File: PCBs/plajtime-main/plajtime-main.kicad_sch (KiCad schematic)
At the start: 84 parts, among them J1 RP SWD, J2 Internal connector, J3 Display connector, J4 Extention connector, J5 Battery connector, J6 Nordic SWD, U1 W25Q64JWU, U2 MP2664, U3 TPS63031DSK, U4 RP2350A, U5 BMA456, U6 MAX17055, U7 RV-3028-C7, U8 nRF52833_QDxx, U9 W25Q64JWU, Y1 13MHz, Y2 32MHz

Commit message: Some layout is done
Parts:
- removed AE1: Antenna_Chip, RF_Antenna:Johanson_2450AT18x100_2400-2500Mhz, symbol Device:Antenna_Chip
- removed C1, C17, C20: 10uF, Capacitor_SMD:C_0402_1005Metric, symbol Device:C
- removed C5: 0.1uF, Capacitor_SMD:C_0201_0603Metric, symbol Device:C
- removed J4: Extention connector, Library:FPC_7, symbol Connector_Generic_MountingPin:Conn_01x07_MountingPin
- removed J5: Battery connector, Library:CONN8_505004-0812_MOL, symbol Connector_Generic_MountingPin:Conn_02x04_Top_Bottom_MountingPin
- removed U1: W25Q64JWU, Package_CSP:WLCSP-8_1.551x2.284mm_Layout2x4_P0.5mm, symbol Memory_Flash:W25Q128JVP
- removed U3: TPS63031DSK, Package_SON:WSON-10-1EP_2.5x2.5mm_P0.5mm_EP1.2x2mm, symbol Regulator_Switching:TPS63031DSK
- added C1: 10uF, Capacitor_SMD:C_0402_1005Metric, symbol Device:C_Small
- added C47: 0.1uF, Capacitor_SMD:C_0201_0603Metric, symbol Device:C_Small
- added C5: 4.7uF, Capacitor_SMD:C_0402_1005Metric, symbol Device:C_Small
- added J4: Extention connector, Library:5050660822, symbol Connector_Generic_MountingPin:Conn_02x04_Odd_Even_MountingPin
- added J5, J7: Conn_Coaxial, Library:W.FL_Hirose_W.FL2-R-SMT-1_Vertical, symbol Connector:Conn_Coaxial
- added J8: Battery Connector, Library:CONN_505066-0622_MOL, symbol Connector_Generic_MountingPin:Conn_02x03_Odd_Even_MountingPin
- added R12: 133k, Resistor_SMD:R_0201_0603Metric, symbol Device:R
- added U1: W25Q64JWBYIM, Library:BGA-24_4x6_6.0x6.0mm, symbol Library:W25Q64JWBYIM
- added U3: TPS628438YKA, Package_BGA:Texas_DSBGA-6_0.757x1.01mm_Layout2x3_P0.35mm, symbol Regulator_Switching:TPS628438YKA
- J1, J6: footprint Connector_PinHeader_1.00mm:PinHeader_1x03_P1.00mm_Vertical -> Library:PinHeader_1x03_P1.00mm_Vertical
- L1: value 1.5uH -> 1uH; LCSC_Part C50325490 -> C223144
- U6: LCSC_Part C2976422 -> (none)
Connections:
- net +3.3V: now also J3.29 (Pin_29), J3.30 (Pin_30), U4.26 (RUN), C47.1, J4.1 (Pin_1), U1.B2 (VCC); no longer C38.1, U8.10 (VBUS)
- net +5V: now also C38.1, U8.10 (VBUS)
- net +BATT: now also U6.B1 (BATT), J8.1 (Pin_1), J8.2 (Pin_2)
- net -BATT: now also J8.5 (Pin_5), J8.6 (Pin_6); no longer U6.11 (CSP)
- net BATT_NTC: now also J8.3 (Pin_3)
- net CLK_OUT: now also U4.37 (GPIO25); no longer U4.35 (GPIO23)
- net DISP_CS: now also U4.15 (GPIO11); no longer U4.19 (GPIO15)
- net DISP_DI1: now also U4.17 (GPIO13); no longer U4.16 (GPIO12)
- net DISP_DI2: now also U4.18 (GPIO14); no longer U4.17 (GPIO13)
- net DISP_DI3: now also U4.19 (GPIO15); no longer U4.18 (GPIO14)
- net DISP_DIO0: now also U4.16 (GPIO12); no longer U4.15 (GPIO11)
- net DISP_RST: now also U4.14 (GPIO10); no longer U4.27 (GPIO16)
- net DISP_SCL: now also U4.28 (GPIO17); no longer U4.14 (GPIO10)
- net DISP_TE: now also U4.5 (GPIO3); no longer U4.29 (GPIO18)
- net EXT_GPIO: now also J4.7 (Pin_7)
- net EXT_INT: now also J4.3 (Pin_3)
- net EXT_RST: now also J4.5 (Pin_5)
- net GND: now also C1.2, C47.2, C5.2, J4.8 (Pin_8), J4.MP (MountPin), J5.2 (Ext), J8.4 (Pin_4), J8.MP (MountPin), R12.2, U1.E3 (GND), U3.A1 (GND)
- net QMI_CS1: no longer U4.60 (QSPI_SS)
- net QMI_SCLK: now also U1.D2 (CLK)
- net QMI_SD0: now also U1.E2 (DI/IO_{0})
- net QMI_SD1: now also U1.C3 (DO/IO_{1})
- net QMI_SD2: now also U1.D3 (~{WP}/IO_{2})
- net QMI_SD3: now also U1.C2 (~{HOLD}/~{RESET}/IO_{3})
- net RP_SCL: now also J2.4 (Pin_4); no longer J2.5 (Pin_5)
- net RP_SDA: now also J2.5 (Pin_5); no longer J2.4 (Pin_4)
- net SCL: now also U8.3 (XL2/P0.01), J4.2 (Pin_2); no longer U8.5 (AIN3/P0.05)
- net SDA: now also U8.2 (XL1/P0.00), J4.4 (Pin_4); no longer U8.4 (AIN2/P0.04)
- net SLIDER_INT: now also U4.36 (GPIO24); no longer U4.34 (GPIO22)
- net TP_INT: now also U4.27 (GPIO16); no longer U4.32 (GPIO20)
- net TP_RESET: now also U4.29 (GPIO18); no longer U4.28 (GPIO17)
- net UART_RX: now also U4.35 (GPIO23)
- net UART_TX: now also U4.34 (GPIO22)
- net VIC_INT: no longer U4.33 (GPIO21)
- net VSYS: now also C5.1, U3.B1 (VIN), U3.C2 (EN); no longer J3.29 (Pin_29), J3.30 (Pin_30)
- net at L1.1: now also U3.B2 (SW)
- net +3V: now reaches L1.2
- net +3V: now also C1.1, U3.A2 (VOS)
- net at L3.1: now also J5.1 (In)
- net at C45.1, U8.22 (NFC1/P0.09): now also J7.1 (In)
- net at C46.1, U8.23 (NFC2/P0.10): now also J7.2 (Ext)
- net at U8.19 (SWDIO): now also J6.3 (Pin_3); no longer J6.2 (Pin_2)
- net at U8.20 (SWDCLK): now also J6.2 (Pin_2); no longer J6.3 (Pin_3)
- new net: R12.1, U3.C1 (VSET)
- new net CSN: U6.A3 (CSN)
- new net CSP: U6.C3 (CSP)
- new net QMI_CS0: U1.B3 (~{CS}), U4.60 (QSPI_SS)
- no-connect marks 9 -> 6
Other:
- moved on the sheet: BT1, C15, C18, C24, C26, C28, C29, C38, C4, C8, J2, J3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

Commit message: Final?
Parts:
- removed TP1: TestPoint, symbol Connector:TestPoint
- added J9: RP USB, Library:PinHeader_1x03_P1.00mm_Vertical, symbol Connector:Conn_01x03_Pin
- U3: footprint Package_BGA:Texas_DSBGA-6_0.757x1.01mm_Layout2x3_P0.35mm -> Library:Texas_DSBGA-6_0.757x1.01mm_Layout2x3_P0.35mm
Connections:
- net +3.3V is gone; now on net +3V: C12.1, C14.1, C16.1, C19.1, C21.1, C22.1, C23.1, C24.1, C25.1, C27.1, C29.1, C3.1, C30.2, C31.1, C32.1, C33.1, C37.1, C47.1, J3.11 (Pin_11), J3.23 (Pin_23), J3.25 (Pin_25), J3.29 (Pin_29), J3.30 (Pin_30), J4.1 (Pin_1), R10.1, R2.1, R7.1, R8.1, R9.1, U1.B2 (VCC), U4.1 (IOVDD), U4.11 (IOVDD), U4.20 (IOVDD), U4.26 (RUN), U4.30 (IOVDD), U4.38 (IOVDD), U4.44 (ADC_AVDD), U4.45 (IOVDD), U4.49 (VREG_VIN), U4.53 (USB_OTP_VDD), U4.54 (QSPI_IOVDD), U5.10 (CSB), U5.3 (VDDIO), U5.7 (VDD), U7.7 (VDD), U8.11 (DECUSB), U8.18 (VDD), U8.30 (VDD), U8.40 (VDD), U8.8 (VDD), U8.9 (VDDH), U9.8 (VCC)
- net EXT_GPIO is gone; now on net SCL: J4.7 (Pin_7)
- net -BATT: now also U6.11 (CSP)
- net CHARGER_INT: now also U8.7 (P0.11); no longer U8.33 (AIN4/P0.28)
- net EXT_INT: now also J4.2 (Pin_2); no longer J4.3 (Pin_3)
- net EXT_RST: now also J4.4 (Pin_4); no longer J4.5 (Pin_5)
- net GAUGE_INT: now also U8.5 (AIN3/P0.05); no longer U8.36 (AIN7/P0.31)
- net GND: now also J9.1 (Pin_1); no longer J6.1 (Pin_1)
- net GPU_INT: now also U8.4 (AIN2/P0.04); no longer U8.17 (P0.20)
- net IMU_INT_1: now also U8.31 (AIN1/P0.03); no longer U8.32 (AIN0/P0.02)
- net IMU_INT_2: now also U8.32 (AIN0/P0.02); no longer U8.31 (AIN1/P0.03)
- net OXY_INT: now also U8.6 (P1.09); no longer U8.7 (P0.11)
- net RTC_INT: now also U8.17 (P0.20); no longer U8.6 (P1.09)
- net SCL: now also J2.2 (Pin_2); no longer J2.3 (Pin_3), J4.2 (Pin_2)
- net SDA: now also J2.3 (Pin_3), J4.5 (Pin_5); no longer J2.2 (Pin_2), J4.4 (Pin_4)
- net SLIDER_INT: now also U4.3 (GPIO1); no longer U4.36 (GPIO24)
- net VIC_INT: now also U4.32 (GPIO20)
- net at U8.16 (P0.18/~{RESET}): now also J6.1 (Pin_1)
- net at U4.24 (SWCLK): now also J1.2 (Pin_2); no longer J1.3 (Pin_3)
- net at U4.25 (SWDIO): now also J1.3 (Pin_3); no longer J1.2 (Pin_2)
- net at U4.51 (USB_DM): now also J9.3 (Pin_3)
- net at U4.52 (USB_DP): now also J9.2 (Pin_2)
- net EXT_GPIO_1: now reaches J4.6 (Pin_6)
- net EXT_GPIO_1: now also U8.36 (AIN7/P0.31)
- net at U8.19 (SWDIO): now also J6.2 (Pin_2); no longer J6.3 (Pin_3)
- net at U8.20 (SWDCLK): now also J6.3 (Pin_3); no longer J6.2 (Pin_2)
- new net EXT_GPIO_2: J4.3 (Pin_3), U8.33 (AIN4/P0.28)
- no-connect marks 6 -> 4
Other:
- moved on the sheet: J1, J4, J6, U9

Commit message: Some small final touches
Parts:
- C34, C35: LCSC_Part (none) -> C541243
- C36: LCSC_Part (none) -> C48642883
- C39: LCSC_Part (none) -> C41361064
- C6, C7: LCSC_Part (none) -> C541244
- J2: LCSC_Part (none) -> C5902841
- J4: LCSC_Part (none) -> C3652707`
- J8: LCSC_Part (none) -> C724122
- R4: LCSC_Part 0402 -> (none)
- U1: LCSC_Part (none) -> C2691929
- U6: LCSC_Part (none) -> C2682627
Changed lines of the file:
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@@
 			)
 		)
+		(property "LCSC_Part" "C2691929"
+			(at 43.18 97.79 0)
+			(effects
+				(font
+					(size 1.27 1.27)
+				)
+				(hide yes)
+			)
+		)
 		(pin "B3"
 		)
@@
 		(on_board yes)
 		(dnp no)
-		(fields_autoplaced yes)
 		(property "Reference" "U6"
 			(at 124.46 180.34 0)
@@
 			)
 		)
+		(property "LCSC_Part" "C2682627"
+			(at 124.46 201.93 0)
+			(effects
+				(font
+					(size 1.27 1.27)
+				)
+				(hide yes)
+			)
+		)
 		(pin "2"
 		)
@@
 			)
 		)
+		(property "LCSC_Part" "C541243"
+			(at 271.78 147.32 90)
+			(effects
+				(font
+					(size 1.27 1.27)
+				)
+				(hide yes)
+			)
+		)
 		(pin "2"
 		)
@@
 			)
 		)
+		(property "LCSC_Part" "C5902841"
+			(at 185.42 252.73 0)
+			(effects
+				(font
+					(size 1.27 1.27)
+				)
+				(hide yes)
+			)
+		)
 		(pin "11"
 		)
@@
 			)
 		)
+		(property "LCSC_Part" "C541244"
+			(at 31.75 165.1 90)
+			(effects
+				(font
+					(size 1.27 1.27)
+				)
+				(hide yes)
+			)
+		)
 		(pin "2"
 		)
@@
 			)
 		)
+		(property "LCSC_Part" "C541243"
+			(at 271.78 137.16 90)
+			(effects
+				(font
+					(size 1.27 1.27)
+				)
+				(hide yes)
+			)
+		)
 		(pin "2"
 		)
@@
 			)
 		)
+		(property "LCSC_Part" "C3652707`"
+			(at 227.33 254 0)
+			(effects
+				(font
+					(size 1.27 1.27)
+				)
+				(hide yes)
+			)
+		)
 		(pin "3"
 		)
@@
 			)
 		)
+		(property "LCSC_Part" "C724122"
+			(at 271.78 254 0)
+			(effects
+				(font
+					(size 1.27 1.27)
+				)
+				(hide yes)
+			)
+		)
 		(pin "2"
 		)
@@
 			)
 		)
+		(property "LCSC_Part" "C41361064"
+			(at 287.02 102.87 0)
+			(effects
+				(font
+					(size 1.27 1.27)
+				)
+				(hide yes)
+			)
+		)
 		(pin "2"
 		)
@@
 			)
 		)
+		(property "LCSC_Part" "C48642883"
+			(at 273.05 102.87 0)
+			(effects
+				(font
+					(size 1.27 1.27)
+				)
+				(hide yes)
+			)
+		)
 		(pin "2"
 		)
@@
 			)
 		)
+		(property "LCSC_Part" "C541244"
+			(at 31.75 154.94 90)
+			(effects
+				(font
+					(size 1.27 1.27)
+				)
+				(hide yes)
+			)
+		)
 		(pin "2"
 		)
@@
 			)
 		)
-		(property "LCSC_Part" "0402"
+		(property "LCSC_Part" " "
 			(at 124.46 223.52 90)
 			(effects

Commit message: Final Main PCB version
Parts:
- C1: renamed from C5; Mouser (none) -> 81-GRM155C80J475MEAJ
- C10: renamed from C11; Mouser (none) -> 81-GRT033R60J104KE1J
- C11: renamed from C12; Mouser (none) -> 81-GRT033R60J104KE1J
- C12: renamed from C13; Mouser (none) -> 81-GRM155C80J475MEAJ
- C13: renamed from C15; Mouser (none) -> 81-GRM155R60J106M05D
- C14, C16, C23: Mouser (none) -> 81-GRT033R60J104KE1J
- C15: renamed from C1; Mouser (none) -> 81-GRM155R60J106M05D
- C17: renamed from C18; Mouser (none) -> 81-GRM155C80J475MEAJ
- C18: renamed from C19; Mouser (none) -> 81-GRT033R60J104KE1J
- C19: renamed from C21; Mouser (none) -> 81-GRT033R60J104KE1J
- C2: renamed from C4; Mouser (none) -> 81-GRM033R61A105ME4J
- C20: renamed from C22; Mouser (none) -> 81-GRT033R60J104KE1J
- C21: renamed from C24; Mouser (none) -> 81-GRT033R60J104KE1J
- C22: renamed from C26; Mouser (none) -> 81-GRT033R60J104KE1J
- C24: renamed from C25; Mouser (none) -> 81-GRT033R60J104KE1J
- C25: renamed from C27; Mouser (none) -> 81-GRT033R60J104KE1J
- C26: renamed from C28; Mouser (none) -> 81-GRM33R60J474KE90D
- C27: renamed from C29; Mouser (none) -> 81-GRT033R60J104KE1J
- C28: renamed from C30; Mouser (none) -> 81-GRT033R60J104KE1J
- C29: renamed from C31; Mouser (none) -> 81-GRM033R61A105ME4J
- C3: renamed from C6; Mouser (none) -> 81-GRT0335C1E150FA2D
- C30: renamed from C32; Mouser (none) -> 81-GRT033R60J104KE1J
- C31: renamed from C33; Mouser (none) -> 81-GRM155C80J475MEAJ
- C32: renamed from C34; Mouser (none) -> 81-GRT0335C1H120FA2D
- C33: renamed from C35; Mouser (none) -> 81-GRT0335C1H120FA2D
- C34: renamed from C36; Mouser (none) -> 791-RF03N1R2B250CT
- C35: renamed from C37; Mouser (none) -> 81-GRM155C80J475MEAJ
- C36: renamed from C47; Mouser (none) -> 81-GRT033R60J104KE1J
- C37: renamed from C39; Mouser (none) -> 791-0201N1R0C250CT
- C38: renamed from C40; Mouser (none) -> 81-GRT033R60J104KE1J
- C39: renamed from C41; Mouser (none) -> 81-GRT033R60J104KE1J
- C4: renamed from C7; Mouser (none) -> 81-GRT0335C1E150FA2D
- C40: renamed from C42; Mouser (none) -> 581-0201YC821K
- C41: renamed from C38; Mouser (none) -> 81-GRM155C80J475MEAJ
- C42: renamed from C43; Mouser (none) -> 81-GRM033R61A105ME4J
- C43: renamed from C44; Mouser (none) -> 81-GRM155C80J475MEAJ
- C44: renamed from C45; value TBD_H -> 270pF_H; LCSC_Part (none) -> C430710; Mouser (none) -> 81-GRM0335C1E271GA1J
- C45: renamed from C46; value TBD_H -> 270pF_H; LCSC_Part (none) -> C430710; Mouser (none) -> 81-GRM0335C1E271GA1J
- C5: renamed from C2; Mouser (none) -> 81-GRT033R60J104KE1J
- C6: renamed from C3; Mouser (none) -> 81-GRM155C80J475MEAJ
- C7: renamed from C8; Mouser (none) -> 81-GRT033R60J104KE1J
- C8: renamed from C9; Mouser (none) -> 81-GRM155C80J475MEAJ
- C9: renamed from C10; Mouser (none) -> 81-GRM155C80J475MEAJ
- J6: renamed from J5; LCSC_Part (none) -> C434809
- J9: renamed from J7; LCSC_Part (none) -> C434809
- R5: renamed from R4; LCSC_Part (none) -> C3024467
- renumbered J9 to J2, J2 to J3, J3 to J4, J4 to J5, J8 to J7, J6 to J8, L2 to L1, L1 to L2, R9 to R10, R10 to R11, R11 to R12, R12 to R2, R2 to R3, R3 to R4, R5 to R6, R6 to R7, R7 to R8, R8 to R9, U9 to U1, U1 to U2, U2 to U4, U4 to U5, U5 to U6, U6 to U7, U7 to U8, U8 to U9
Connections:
- no-connect marks 4 -> 14
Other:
- note added: "275.52pF"
- note removed: "TBD"

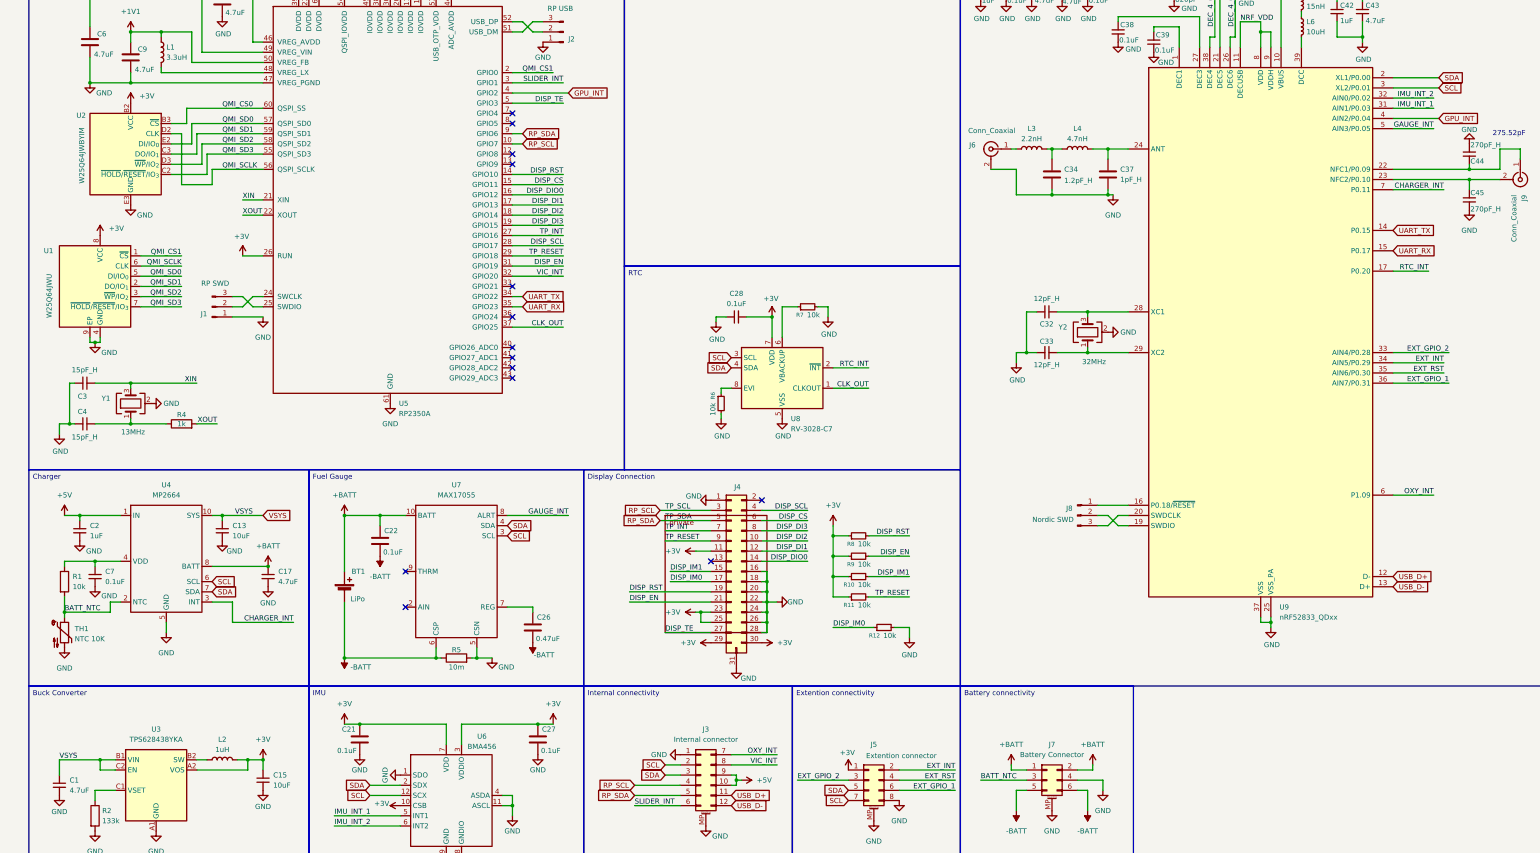
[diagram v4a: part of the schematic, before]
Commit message: feat: Add new KiCad project for battery flexible PCB, updating main, auxiliary, and 3D models.
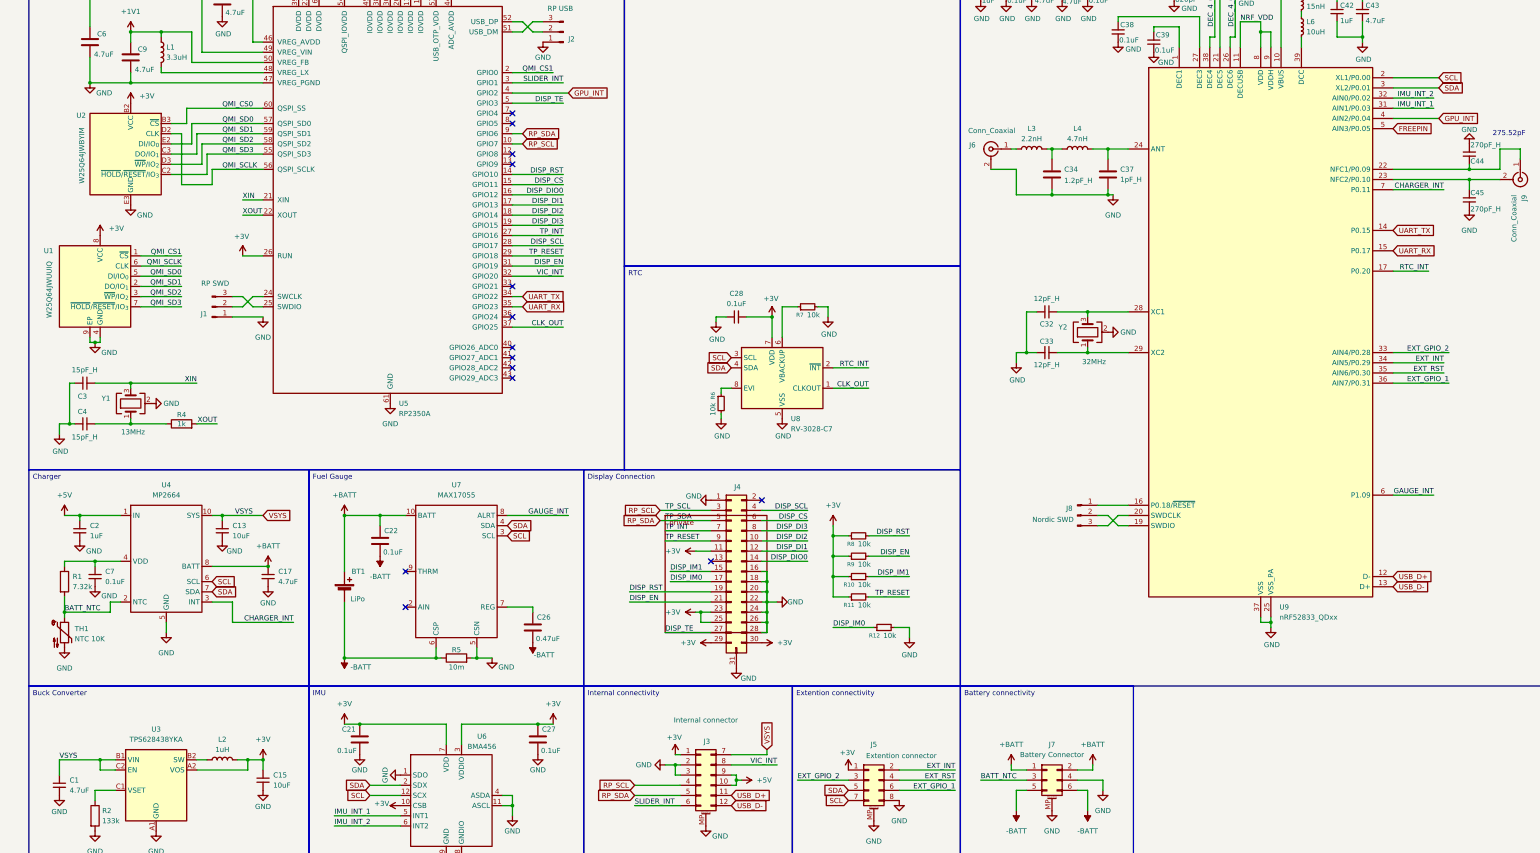
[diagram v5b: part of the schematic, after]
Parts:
- BT1: now left out of the parts list
- C1, C12, C17, C31, C35, C41, C43, C6, C8, C9: Mouser 81-GRM155C80J475MEAJ -> (none)
- C10, C11, C14, C16, C18, C19, C20, C21, C22, C23, C24, C25, C27, C28, C30, C36, C38, C39, C5, C7: Mouser 81-GRT033R60J104KE1J -> (none)
- C13, C15: Mouser 81-GRM155R60J106M05D -> (none)
- C2, C29, C42: Mouser 81-GRM033R61A105ME4J -> (none)
- C26: Mouser 81-GRM33R60J474KE90D -> (none)
- C3, C4: Mouser 81-GRT0335C1E150FA2D -> (none)
- C32, C33: Mouser 81-GRT0335C1H120FA2D -> (none)
- C34: Mouser 791-RF03N1R2B250CT -> (none)
- C37: Mouser 791-0201N1R0C250CT -> (none)
- C40: Mouser 581-0201YC821K -> (none)
- C44, C45: Mouser 81-GRM0335C1E271GA1J -> (none)
- J5: LCSC_Part C3652707` -> C3652707
- J8: footprint Library:PinHeader_1x03_P1.00mm_Vertical -> Library:PinHeader_1x03_P1.00mm_Vertical_1
- L1: LCSC_Part C86107 -> C48945007
- R1: value 10k -> 7.32k; LCSC_Part C106225 -> C321025
- U1: value W25Q64JWU -> W25Q64JWUUIQ; LCSC_Part C190862 -> (none); Mouser (none) -> 454-W25Q64JWUUIQTR
- U4: LCSC_Part MOUSER ONLY -> (none); Mouser (none) -> 946-MP2664GG-0000-P
- U5: LCSC_Part C42411118 -> (none); Mouser (none) -> 358-SC150913
- U6: LCSC_Part C189518 -> (none)
- U7: LCSC_Part C2682627 -> C2976422
- U9: LCSC_Part C2895249 -> (none); Mouser (none) -> 949-NRF52833-QDAA-R
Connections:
- net +3V: now also J3.1 (Pin_1)
- net GAUGE_INT: now also U9.6 (P1.09); no longer U9.5 (AIN3/P0.05)
- net GND: now also J3.2 (Pin_2), J3.3 (Pin_3); no longer J3.1 (Pin_1)
- net SCL: now also U9.2 (XL1/P0.00); no longer J3.2 (Pin_2), U9.3 (XL2/P0.01)
- net SDA: now also U9.3 (XL2/P0.01); no longer J3.3 (Pin_3), U9.2 (XL1/P0.00)
- net VSYS: now also J3.7 (Pin_7)
- removed net OXY_INT: J3.7 (Pin_7), U9.6 (P1.09)
- new net FREEPIN: U9.5 (AIN3/P0.05)

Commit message: Formal remarks, added usb pins holder to model
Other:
- note added: "PLAJTA"
- title: (none) -> PlajTime Příloha 1 - Schéma zapojení
